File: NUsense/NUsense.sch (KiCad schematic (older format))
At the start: 0 parts

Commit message: Update NUsense Files
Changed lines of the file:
@@
 LIBS:NUbots
 LIBS:STM32F746ZGT6
+LIBS:Header_Connectors
 LIBS:NUsense-cache
 EELAYER 25 0
@@
 $Descr A3 16535 11693
 encoding utf-8
-Sheet 1 4
+Sheet 1 9
 Title ""
 Date ""
@@
 F1 "Switches.sch" 60
 $EndSheet
+$Sheet
+S 7050 900  1750 1150
+U 5A698B54
+F0 "RS485" 60
+F1 "RS485.sch" 60
+$EndSheet
+$Sheet
+S 9250 900  1450 1150
+U 5A69B431
+F0 "Power" 60
+F1 "Power.sch" 60
+$EndSheet
+$Sheet
+S 11200 900  1600 1150
+U 5A6A6784
+F0 "OTG-HS USB2o0" 60
+F1 "OTG-HS USB2o0.sch" 60
+$EndSheet
+$Sheet
+S 13250 1000 1600 1100
+U 5A6A8404
+F0 "UART_LED" 60
+F1 "UART_LED.sch" 60
+$EndSheet
+$Sheet
+S 900  2700 1800 1250
+U 5A6D6234
+F0 "Voltage_Sensor" 60
+F1 "Voltage_Sensor.sch" 60
+$EndSheet
 $EndSCHEMATC

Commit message: Change hierarchy layout
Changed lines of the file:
@@
 LIBS:valves
 LIBS:ADM6713RAKS
+LIBS:Header_Connectors
 LIBS:MPU6000
 LIBS:NUbots
 LIBS:STM32F746ZGT6
-LIBS:Header_Connectors
 LIBS:NUsense-cache
 EELAYER 25 0
@@
 $EndDescr
 $Sheet
-S 2950 850  1800 1250
+S 12300 1900 1850 1300
 U 5A6BC0DA
-F0 "MPU Sensor" 60
-F1 "MPU Sensor.sch" 60
+F0 "MPU Sensor" 118
+F1 "MPU Sensor.sch" 118
+F2 "MPU_SCL" O L 12300 2050 60
+F3 "MPU_SDA?SDI" O L 12300 2150 60
+F4 "MPU_INT" O L 12300 2250 60
 $EndSheet
 $Sheet
-S 850  850  1850 1300
+S 7700 3050 3250 2450
 U 5A6C107A
-F0 "MCU Unit" 60
-F1 "MCU Unit.sch" 60
+F0 "MCU Unit" 118
+F1 "MCU Unit.sch" 118
+F2 "MPU_INT" I L 7700 3150 60
+F3 "MPU_SDA/SDI" I L 7700 3250 60
+F4 "MPU_SCL" I L 7700 3350 60
+F5 "MCU_RESET" I L 7700 3700 60
+F6 "OTG_HS_ULPI_STP" B L 7700 4900 60
+F7 "OTG_HS_ULPI_DIR" B L 7700 5000 60
+F8 "OTG_HS_ULPI_NXT" B L 7700 5100 60
+F9 "OTG_HS_ULPI_CK" B L 7700 5200 60
+F10 "JTD0_SW0" B L 7700 4050 60
+F11 "JTDI" B L 7700 4350 60
+F12 "JTCK_SWCLK" B L 7700 4150 60
+F13 "JTMS_SWDIO" B L 7700 4250 60
+F14 "USART1_TX" O R 10950 3450 60
+F15 "USART1_RX" I R 10950 3550 60
+F16 "USART6_TX" O R 10950 4800 60
+F17 "USART6_RX" I R 10950 4900 60
+F18 "USART3_RX" I R 10950 4100 60
+F19 "USART3_TX" O R 10950 4000 60
+F20 "UART5_TX" O R 10950 4500 60
+F21 "USART2_TX" O R 10950 3700 60
+F22 "UART5_RX" I R 10950 4600 60
+F23 "UART8_TX" O R 10950 5350 60
+F24 "USART2_RX" I R 10950 3800 60
+F25 "UART8_RX" I R 10950 5450 60
+F26 "UART7_TX" O R 10950 5100 60
+F27 "UART7_RX" I R 10950 5200 60
 $EndSheet
 $Sheet
-S 5250 900  1100 1000
+S 2950 7350 1850 1300
 U 5A6C1205
-F0 "Switches" 60
-F1 "Switches.sch" 60
+F0 "Switches" 118
+F1 "Switches.sch" 118
+F2 "BUZZER_SIG" I R 4800 7450 60
+F3 "MCU_RESET" O R 4800 7550 60
 $EndSheet
 $Sheet
-S 7050 900  1750 1150
+S 12450 7650 1850 1300
 U 5A698B54
-F0 "RS485" 60
-F1 "RS485.sch" 60
+F0 "RS485" 118
+F1 "RS485.sch" 118
+F2 "DXL_RXD" B L 12450 7750 60
+F3 "DXL_TXD" B L 12450 7850 60
+F4 "DXL_DIR" I L 12450 7950 60
 $EndSheet
 $Sheet
-S 9250 900  1450 1150
+S 7700 6150 1850 1300
 U 5A69B431
-F0 "Power" 60
-F1 "Power.sch" 60
+F0 "Power" 118
+F1 "Power.sch" 118
 $EndSheet
 $Sheet
-S 11200 900  1600 1150
+S 2850 2000 1850 1300
 U 5A6A6784
-F0 "OTG-HS USB2o0" 60
-F1 "OTG-HS USB2o0.sch" 60
+F0 "OTG-HS USB2o0" 118
+F1 "OTG-HS USB2o0.sch" 118
+F2 "OTG_HS_ULPI_STP" B R 4700 2100 60
+F3 "OTG_HS_ULPI_NXT" B R 4700 2200 60
+F4 "OTG_HS_ULPI_DIR" B R 4700 2300 60
 $EndSheet
 $Sheet
-S 13250 1000 1600 1100
+S 12350 4850 1850 1300
 U 5A6A8404
-F0 "UART_LED" 60
-F1 "UART_LED.sch" 60
+F0 "UART_LED" 118
+F1 "UART_LED.sch" 118
+F2 "USER_UART_RX" I L 12350 4950 60
+F3 "USER_UART_TX" O L 12350 5050 60
 $EndSheet
 $Sheet
-S 900  2700 1800 1250
+S 2850 4650 1850 1300
 U 5A6D6234
-F0 "Voltage_Sensor" 60
-F1 "Voltage_Sensor.sch" 60
+F0 "Voltage_Sensor" 118
+F1 "Voltage_Sensor.sch" 118
+F2 "I_OUT" O R 4700 4800 60
 $EndSheet
 $EndSCHEMATC

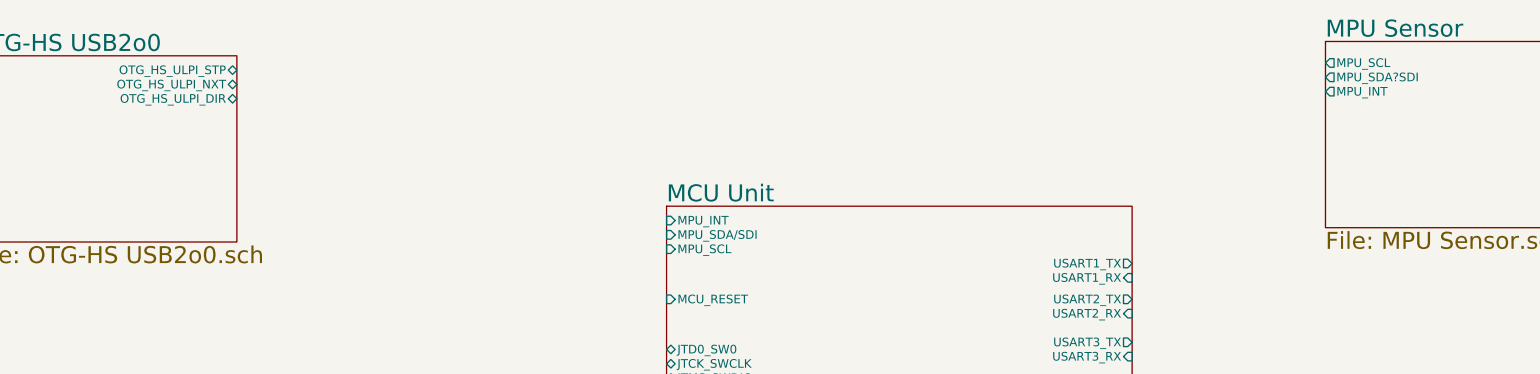
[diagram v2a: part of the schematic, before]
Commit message: Update component values
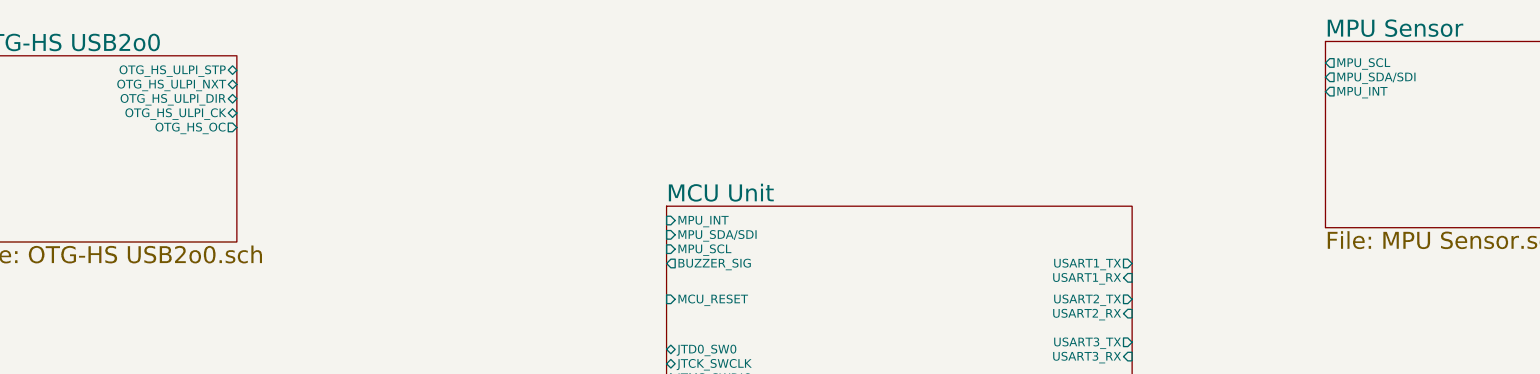
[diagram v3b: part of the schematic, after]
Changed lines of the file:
@@
 F1 "MPU Sensor.sch" 118
 F2 "MPU_SCL" O L 12300 2050 60
-F3 "MPU_SDA?SDI" O L 12300 2150 60
-F4 "MPU_INT" O L 12300 2250 60
+F3 "MPU_INT" O L 12300 2250 60
+F4 "MPU_SDA/SDI" O L 12300 2150 60
 $EndSheet
 $Sheet
@@
 F26 "UART7_TX" O R 10950 5100 60
 F27 "UART7_RX" I R 10950 5200 60
+F28 "BUZZER_SIG" O L 7700 3450 60
 $EndSheet
 $Sheet
@@
 F3 "OTG_HS_ULPI_NXT" B R 4700 2200 60
 F4 "OTG_HS_ULPI_DIR" B R 4700 2300 60
+F5 "OTG_HS_ULPI_CK" B R 4700 2400 60
+F6 "OTG_HS_OC" O R 4700 2500 60
 $EndSheet
 $Sheet

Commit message: Correct Broken Files
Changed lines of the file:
@@
 F3 "DXL_TXD" B L 12450 7850 60
 F4 "DXL_DIR" I L 12450 7950 60
+F5 "DXL_PWR" I L 12450 8050 60
 $EndSheet
 $Sheet
@@
 F0 "Power" 118
 F1 "Power.sch" 118
+F2 "DXL_PWR" O R 9550 6300 60
 $EndSheet
 $Sheet
@@
 F1 "Voltage_Sensor.sch" 118
 F2 "I_OUT" O R 4700 4800 60
+F3 "VS_SCL" I R 4700 5100 60
+F4 "VS_SDA" I R 4700 5200 60
+F5 "VS_ALERT" O R 4700 5300 60
 $EndSheet
 $EndSCHEMATC

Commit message: Main page additions
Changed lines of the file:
@@
 F5 "MCU_RESET" I L 7700 3700 60
 F6 "OTG_HS_ULPI_STP" B L 7700 4900 60
-F7 "OTG_HS_ULPI_DIR" B L 7700 5000 60
-F8 "OTG_HS_ULPI_NXT" B L 7700 5100 60
+F7 "OTG_HS_ULPI_DIR" B L 7700 5100 60
+F8 "OTG_HS_ULPI_NXT" B L 7700 5000 60
 F9 "OTG_HS_ULPI_CK" B L 7700 5200 60
 F10 "JTD0_SW0" B L 7700 4050 60
@@
 F27 "UART7_RX" I R 10950 5200 60
 F28 "BUZZER_SIG" O L 7700 3450 60
+F29 "I2C4_SDA" B L 7700 4550 60
+F30 "I2C4_INT" B L 7700 4750 60
+F31 "I2C4_SCL" B L 7700 4650 60
 $EndSheet
 $Sheet
@@
 F1 "Voltage_Sensor.sch" 118
 F2 "I_OUT" O R 4700 4800 60
-F3 "VS_SCL" I R 4700 5100 60
-F4 "VS_SDA" I R 4700 5200 60
+F3 "VS_SCL" I R 4700 5200 60
+F4 "VS_SDA" I R 4700 5100 60
 F5 "VS_ALERT" O R 4700 5300 60
 $EndSheet
+Wire Wire Line
+	4800 7550 6300 7550
+Wire Wire Line
+	5900 4550 7700 4550
+Wire Wire Line
+	4700 2100 7000 2100
+Wire Wire Line
+	7000 2100 7000 4900
+Wire Wire Line
+	7000 4900 7700 4900
+Wire Wire Line
+	4700 2200 6900 2200
+Wire Wire Line
+	4700 2300 6800 2300
+Wire Wire Line
+	6800 2300 6800 5100
+Wire Wire Line
+	4700 2400 6700 2400
+Wire Wire Line
+	6700 2400 6700 5200
+Wire Wire Line
+	6700 5200 7700 5200
+Wire Wire Line
+	9550 6300 10800 6300
+Wire Wire Line
+	10800 6300 10800 8050
+Wire Wire Line
+	10800 8050 12450 8050
+Wire Wire Line
+	7700 3150 7600 3150
+Wire Wire Line
+	7600 3150 7600 2250
+Wire Wire Line
+	7600 2250 12300 2250
+Wire Wire Line
+	12300 2150 7500 2150
+Wire Wire Line
+	7500 2150 7500 3250
+Wire Wire Line
+	7500 3250 7700 3250
+Wire Wire Line
+	7700 3350 7400 3350
+Wire Wire Line
+	7400 3350 7400 2050
+Wire Wire Line
+	7400 2050 12300 2050
+Wire Wire Line
+	6200 3450 7700 3450
+Wire Wire Line
+	4700 5300 6100 5300
+Wire Wire Line
+	6200 7450 6200 3450
+Wire Wire Line
+	6300 7550 6300 3700
+Wire Wire Line
+	6200 7450 4800 7450
+Wire Wire Line
+	6300 3700 7700 3700
+Wire Wire Line
+	6000 4650 6000 5200
+Wire Wire Line
+	6000 4650 7700 4650
+Wire Wire Line
+	6100 5300 6100 4750
+Wire Wire Line
+	6100 4750 7700 4750
+Wire Wire Line
+	6000 5200 4700 5200
+Wire Wire Line
+	4700 5100 5900 5100
+Wire Wire Line
+	5900 5100 5900 4550
+Wire Wire Line
+	6800 5100 7700 5100
+Wire Wire Line
+	7700 5000 6900 5000
+Wire Wire Line
+	6900 5000 6900 2200
 $EndSCHEMATC

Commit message: Update connections
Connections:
- wire segments 39 -> 94

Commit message: Footprints
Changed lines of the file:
@@
 F28 "BUZZER_SIG" O L 7200 2600 60
 F29 "I2C4_SDA" B L 7200 3700 60
-F30 "I2C4_INT" B L 7200 3900 60
-F31 "I2C4_SCL" B L 7200 3800 60
+F30 "I2C4_SCL" B L 7200 3800 60
+F31 "VS_ALERT" B L 7200 3900 60
 $EndSheet
 $Sheet

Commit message: ESD protection
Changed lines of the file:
@@
 F5 "OTG_HS_ULPI_CK" B R 4200 1550 60
 F6 "OTG_HS_OC" O R 4200 1650 60
+F7 "USB_~ACK" I R 4200 1750 60
 $EndSheet
 $Sheet
